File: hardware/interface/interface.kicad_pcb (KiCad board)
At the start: 2 copper layers, 44.4 x 35.6 mm, 7 parts, among them J1 Board Connector, SW1 Rotary_Encoder_Switch, U1 128x32_OLED, U2 MCP23018-E_SS

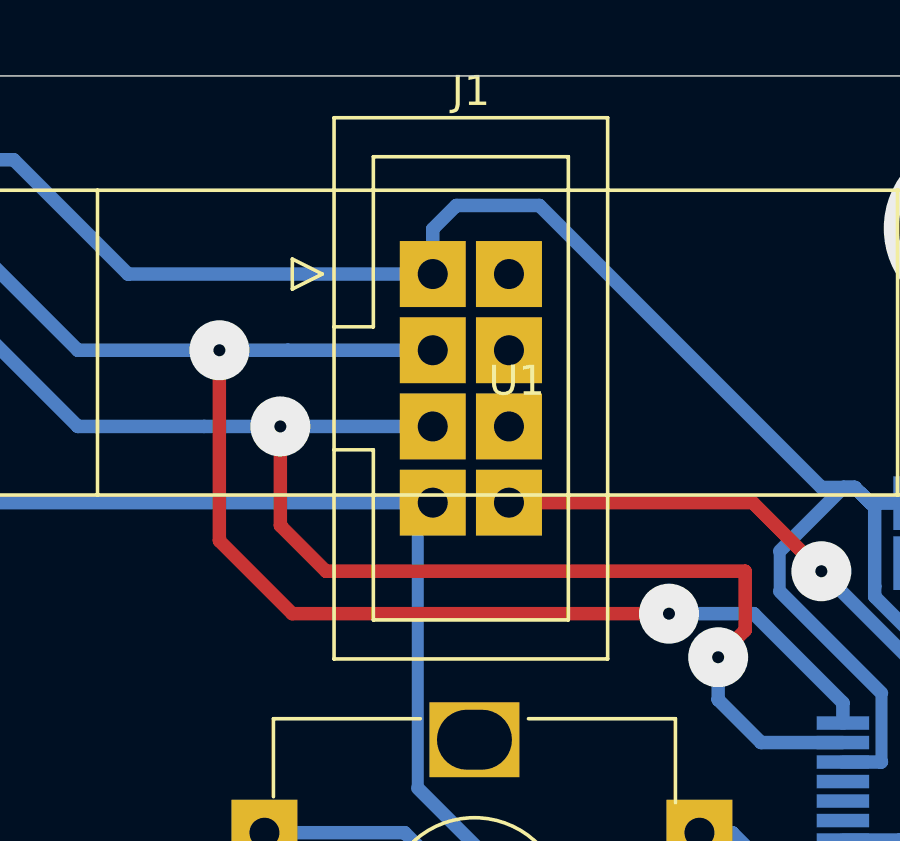
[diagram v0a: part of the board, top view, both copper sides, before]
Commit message: Whoops; the connector should be on the back side of the board.
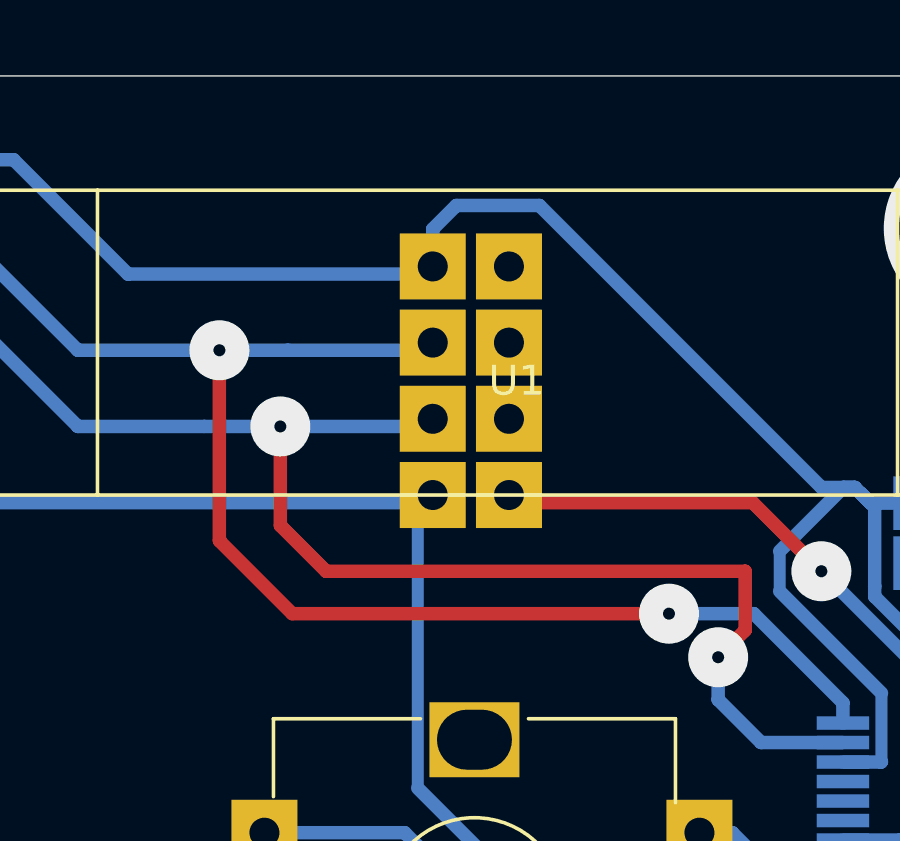
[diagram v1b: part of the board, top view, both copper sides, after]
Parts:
- J1: moved to B.Cu
- moved J1 7.37 mm to (138.2, 72.4)
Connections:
- J1 pad 1: +5V -> GND
- J1 pad 2: (no net) -> INT
- J1 pad 3: SDA -> SCL
- J1 pad 5: SCL -> SDA
- J1 pad 7: GND -> +5V
- J1 pad 8: INT -> (no net)
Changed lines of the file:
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@@
     (add_net GND)
     (add_net INT)
+    (add_net "Net-(J1-Pad4)")
+    (add_net "Net-(J1-Pad6)")
+    (add_net "Net-(J1-Pad8)")
     (add_net "Net-(R1-Pad2)")
     (add_net "Net-(SW1-PadA)")
@@
     (add_net "Net-(SW1-PadS1)")
     (add_net "Net-(SW1-PadS2)")
+    (add_net "Net-(U2-Pad16)")
+    (add_net "Net-(U2-Pad17)")
+    (add_net "Net-(U2-Pad18)")
+    (add_net "Net-(U2-Pad19)")
+    (add_net "Net-(U2-Pad20)")
+    (add_net "Net-(U2-Pad21)")
+    (add_net "Net-(U2-Pad22)")
+    (add_net "Net-(U2-Pad23)")
+    (add_net "Net-(U2-Pad24)")
+    (add_net "Net-(U2-Pad7)")
+    (add_net "Net-(U2-Pad8)")
+    (add_net "Net-(U2-Pad9)")
     (add_net SCL)
     (add_net SDA)
   )
-  (module Connector_IDC:IDC-Header_2x04_P2.54mm_Vertical (layer F.Cu)
-    (at 138.176 65.024)
+  (module Connector_IDC:IDC-Header_2x04_P2.54mm_Vertical (layer B.Cu)
+    (at 138.176 72.39)
     (descr "Through hole IDC box header, 2x04, 2.54mm pitch, DIN 41651 / IEC 60603-13, double rows, https://docs.google.com/spreadsheets/d/16SsEcesNF15N3Lb4niX7dcUr-NY5_MFPQhobNuNppn4/edit#gid=0")
     (tags "Through hole vertical IDC box header THT 2x04 2.54mm double row")
-    (fp_text reference J1 (at 1.27 -6.1) (layer F.SilkS)
-      (effects (font (size 1 1) (thickness 0.15)))
+    (fp_text reference J1 (at 1.27 6.1) (layer B.SilkS)
+      (effects (font (size 1 1) (thickness 0.15)) (justify mirror))
     )
-    (fp_text value "Board Connector" (at 1.27 13.72) (layer F.Fab)
-      (effects (font (size 1 1) (thickness 0.15)))
+    (fp_text value "Board Connector" (at 1.27 -13.72) (layer B.Fab)
+      (effects (font (size 1 1) (thickness 0.15)) (justify mirror))
     )
-    (fp_line (start -3.18 -4.1) (end -2.18 -5.1) (layer F.Fab) (width 0.1))
-    (fp_line (start -2.18 -5.1) (end 5.72 -5.1) (layer F.Fab) (width 0.1))
-    (fp_line (start 5.72 -5.1) (end 5.72 12.72) (layer F.Fab) (width 0.1))
-    (fp_line (start 5.72 12.72) (end -3.18 12.72) (layer F.Fab) (width 0.1))
-    (fp_line (start -3.18 12.72) (end -3.18 -4.1) (layer F.Fab) (width 0.1))
-    (fp_line (start -3.18 1.76) (end -1.98 1.76) (layer F.Fab) (width 0.1))
-    (fp_line (start -1.98 1.76) (end -1.98 -3.91) (layer F.Fab) (width 0.1))
-    (fp_line (start -1.98 -3.91) (end 4.52 -3.91) (layer F.Fab) (width 0.1))
-    (fp_line (start 4.52 -3.91) (end 4.52 11.53) (layer F.Fab) (width 0.1))
-    (fp_line (start 4.52 11.53) (end -1.98 11.53) (layer F.Fab) (width 0.1))
-    (fp_line (start -1.98 11.53) (end -1.98 5.86) (layer F.Fab) (width 0.1))
-    (fp_line (start -1.98 5.86) (end -1.98 5.86) (layer F.Fab) (width 0.1))
-    (fp_line (start -1.98 5.86) (end -3.18 5.86) (layer F.Fab) (width 0.1))
-    (fp_line (start -3.29 -5.21) (end 5.83 -5.21) (layer F.SilkS) (width 0.12))
-    (fp_line (start 5.83 -5.21) (end 5.83 12.83) (layer F.SilkS) (width 0.12))
-    (fp_line (start 5.83 12.83) (end -3.29 12.83) (layer F.SilkS) (width 0.12))
-    (fp_line (start -3.29 12.83) (end -3.29 -5.21) (layer F.SilkS) (width 0.12))
-    (fp_line (start -3.29 1.76) (end -1.98 1.76) (layer F.SilkS) (width 0.12))
-    (fp_line (start -1.98 1.76) (end -1.98 -3.91) (layer F.SilkS) (width 0.12))
-    (fp_line (start -1.98 -3.91) (end 4.52 -3.91) (layer F.SilkS) (width 0.12))
-    (fp_line (start 4.52 -3.91) (end 4.52 11.53) (layer F.SilkS) (width 0.12))
-    (fp_line (start 4.52 11.53) (end -1.98 11.53) (layer F.SilkS) (width 0.12))
-    (fp_line (start -1.98 11.53) (end -1.98 5.86) (layer F.SilkS) (width 0.12))
-    (fp_line (start -1.98 5.86) (end -1.98 5.86) (layer F.SilkS) (width 0.12))
-    (fp_line (start -1.98 5.86) (end -3.29 5.86) (layer F.SilkS) (width 0.12))
-    (fp_line (start -3.68 0) (end -4.68 -0.5) (layer F.SilkS) (width 0.12))
-    (fp_line (start -4.68 -0.5) (end -4.68 0.5) (layer F.SilkS) (width 0.12))
-    (fp_line (start -4.68 0.5) (end -3.68 0) (layer F.SilkS) (width 0.12))
-    (fp_line (start -3.68 -5.6) (end -3.68 13.22) (layer F.CrtYd) (width 0.05))
-    (fp_line (start -3.68 13.22) (end 6.22 13.22) (layer F.CrtYd) (width 0.05))
-    (fp_line (start 6.22 13.22) (end 6.22 -5.6) (layer F.CrtYd) (width 0.05))
-    (fp_line (start 6.22 -5.6) (end -3.68 -5.6) (layer F.CrtYd) (width 0.05))
-    (fp_text user %R (at 1.27 3.81 90) (layer F.Fab)
-      (effects (font (size 1 1) (thickness 0.15)))
+    (fp_line (start -3.18 4.1) (end -2.18 5.1) (layer B.Fab) (width 0.1))
+    (fp_line (start -2.18 5.1) (end 5.72 5.1) (layer B.Fab) (width 0.1))
+    (fp_line (start 5.72 5.1) (end 5.72 -12.72) (layer B.Fab) (width 0.1))
+    (fp_line (start 5.72 -12.72) (end -3.18 -12.72) (layer B.Fab) (width 0.1))
+    (fp_line (start -3.18 -12.72) (end -3.18 4.1) (layer B.Fab) (width 0.1))
+    (fp_line (start -3.18 -1.76) (end -1.98 -1.76) (layer B.Fab) (width 0.1))
+    (fp_line (start -1.98 -1.76) (end -1.98 3.91) (layer B.Fab) (width 0.1))
+    (fp_line (start -1.98 3.91) (end 4.52 3.91) (layer B.Fab) (width 0.1))
+    (fp_line (start 4.52 3.91) (end 4.52 -11.53) (layer B.Fab) (width 0.1))
+    (fp_line (start 4.52 -11.53) (end -1.98 -11.53) (layer B.Fab) (width 0.1))
+    (fp_line (start -1.98 -11.53) (end -1.98 -5.86) (layer B.Fab) (width 0.1))
+    (fp_line (start -1.98 -5.86) (end -1.98 -5.86) (layer B.Fab) (width 0.1))
+    (fp_line (start -1.98 -5.86) (end -3.18 -5.86) (layer B.Fab) (width 0.1))
+    (fp_line (start -3.29 5.21) (end 5.83 5.21) (layer B.SilkS) (width 0.12))
+    (fp_line (start 5.83 5.21) (end 5.83 -12.83) (layer B.SilkS) (width 0.12))
+    (fp_line (start 5.83 -12.83) (end -3.29 -12.83) (layer B.SilkS) (width 0.12))
+    (fp_line (start -3.29 -12.83) (end -3.29 5.21) (layer B.SilkS) (width 0.12))
+    (fp_line (start -3.29 -1.76) (end -1.98 -1.76) (layer B.SilkS) (width 0.12))
+    (fp_line (start -1.98 -1.76) (end -1.98 3.91) (layer B.SilkS) (width 0.12))
+    (fp_line (start -1.98 3.91) (end 4.52 3.91) (layer B.SilkS) (width 0.12))
+    (fp_line (start 4.52 3.91) (end 4.52 -11.53) (layer B.SilkS) (width 0.12))
+    (fp_line (start 4.52 -11.53) (end -1.98 -11.53) (layer B.SilkS) (width 0.12))
+    (fp_line (start -1.98 -11.53) (end -1.98 -5.86) (layer B.SilkS) (width 0.12))
+    (fp_line (start -1.98 -5.86) (end -1.98 -5.86) (layer B.SilkS) (width 0.12))
+    (fp_line (start -1.98 -5.86) (end -3.29 -5.86) (layer B.SilkS) (width 0.12))
+    (fp_line (start -3.68 0) (end -4.68 0.5) (layer B.SilkS) (width 0.12))
+    (fp_line (start -4.68 0.5) (end -4.68 -0.5) (layer B.SilkS) (width 0.12))
+    (fp_line (start -4.68 -0.5) (end -3.68 0) (layer B.SilkS) (width 0.12))
+    (fp_line (start -3.68 5.6) (end -3.68 -13.22) (layer B.CrtYd) (width 0.05))
+    (fp_line (start -3.68 -13.22) (end 6.22 -13.22) (layer B.CrtYd) (width 0.05))
+    (fp_line (start 6.22 -13.22) (end 6.22 5.6) (layer B.CrtYd) (width 0.05))
+    (fp_line (start 6.22 5.6) (end -3.68 5.6) (layer B.CrtYd) (width 0.05))
+    (fp_text user %R (at 1.27 -3.81 -90) (layer B.Fab)
+      (effects (font (size 1 1) (thickness 0.15)) (justify mirror))
     )
-    (pad 8 thru_hole rect (at 2.54 7.62) (size 2.2 2.2) (drill 1) (layers *.Cu *.Mask)
+    (pad 8 thru_hole rect (at 2.54 -7.62) (size 2.2 2.2) (drill 1) (layers *.Cu *.Mask))
+    (pad 6 thru_hole rect (at 2.54 -5.08) (size 2.2 2.2) (drill 1) (layers *.Cu *.Mask))
+    (pad 4 thru_hole rect (at 2.54 -2.54) (size 2.2 2.2) (drill 1) (layers *.Cu *.Mask))
+    (pad 2 thru_hole rect (at 2.54 0) (size 2.2 2.2) (drill 1) (layers *.Cu *.Mask)
       (net 4 INT))
-    (pad 6 thru_hole rect (at 2.54 5.08) (size 2.2 2.2) (drill 1) (layers *.Cu *.Mask))
-    (pad 4 thru_hole rect (at 2.54 2.54) (size 2.2 2.2) (drill 1) (layers *.Cu *.Mask))
-    (pad 2 thru_hole rect (at 2.54 0) (size 2.2 2.2) (drill 1) (layers *.Cu *.Mask))
-    (pad 7 thru_hole rect (at 0 7.62) (size 2.2 2.2) (drill 1) (layers *.Cu *.Mask)
+    (pad 7 thru_hole rect (at 0 -7.62) (size 2.2 2.2) (drill 1) (layers *.Cu *.Mask)
+      (net 1 +5V))
+    (pad 5 thru_hole rect (at 0 -5.08) (size 2.2 2.2) (drill 1) (layers *.Cu *.Mask)
+      (net 3 SDA))
+    (pad 3 thru_hole rect (at 0 -2.54) (size 2.2 2.2) (drill 1) (layers *.Cu *.Mask)
+      (net 5 SCL))
+    (pad 1 thru_hole rect (at 0 0) (size 2.2 2.2) (drill 1) (layers *.Cu *.Mask)
       (net 2 GND))
-    (pad 5 thru_hole rect (at 0 5.08) (size 2.2 2.2) (drill 1) (layers *.Cu *.Mask)
-      (net 5 SCL))
-    (pad 3 thru_hole rect (at 0 2.54) (size 2.2 2.2) (drill 1) (layers *.Cu *.Mask)
-      (net 3 SDA))
-    (pad 1 thru_hole rect (at 0 0) (size 2.2 2.2) (drill 1) (layers *.Cu *.Mask)
-      (net 1 +5V))
     (model ${KISYS3DMOD}/Connector_IDC.3dshapes/IDC-Header_2x04_P2.54mm_Vertical.wrl
       (at (xyz 0 0 0))

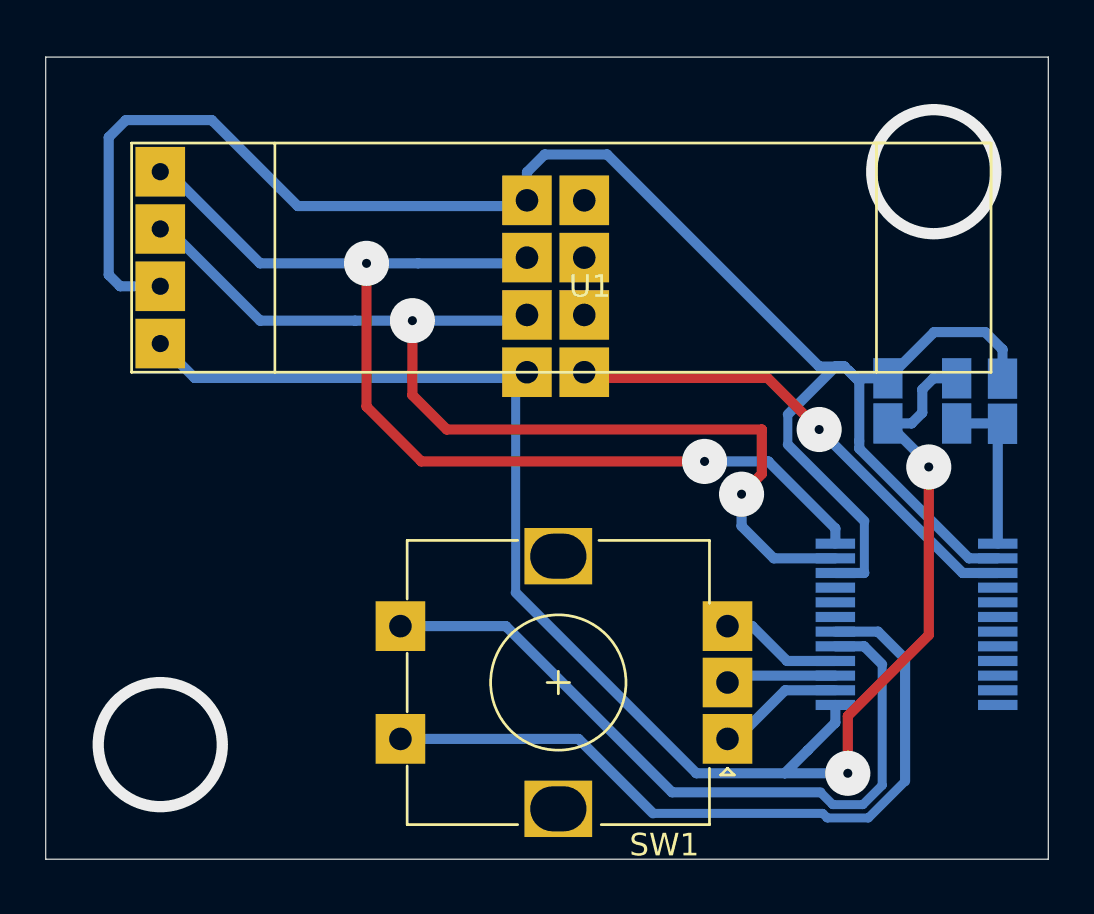
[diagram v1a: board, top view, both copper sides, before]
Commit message: Updating interface PCB.
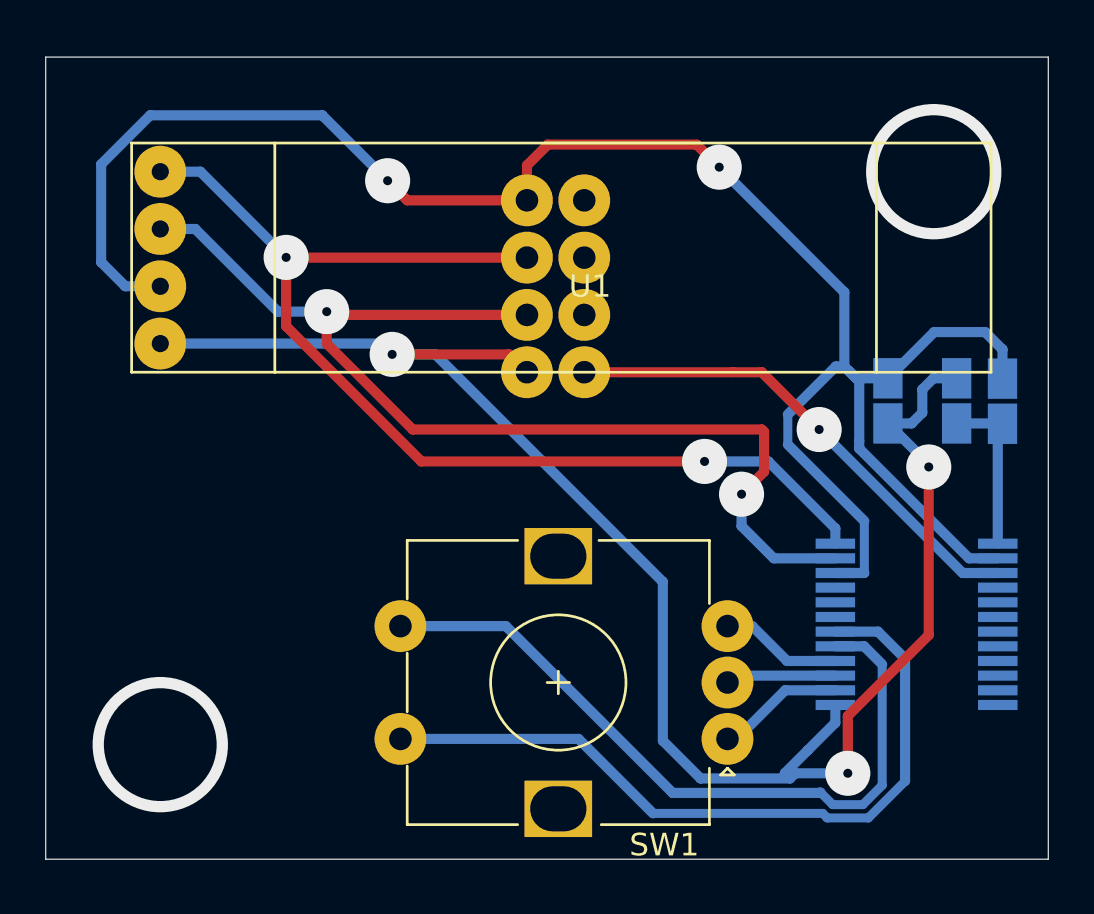
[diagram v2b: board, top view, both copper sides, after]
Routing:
- net GND: track 70.8 -> 75.6 mm, vias 2 -> 3
- net SCL: track 46.8 -> 49.6 mm
- net +5V: track 83.4 -> 85.3 mm, vias 0 -> 2
- net SDA: track 48.0 -> 49.6 mm
